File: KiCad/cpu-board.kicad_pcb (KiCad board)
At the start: 2 copper layers, 100 x 100 mm, 15 parts, among them SW1 SW_PUSH_SMALL, U1 29F040B, U10 74LS377, U11 GAL22V10, U2 68008D, U3 74LS00, U4 BS62LV4006, U5 74LS08, U6 74LS139, U7 74LS32, U8 74LS244, U9 LM555, X1 OSCILLATOR

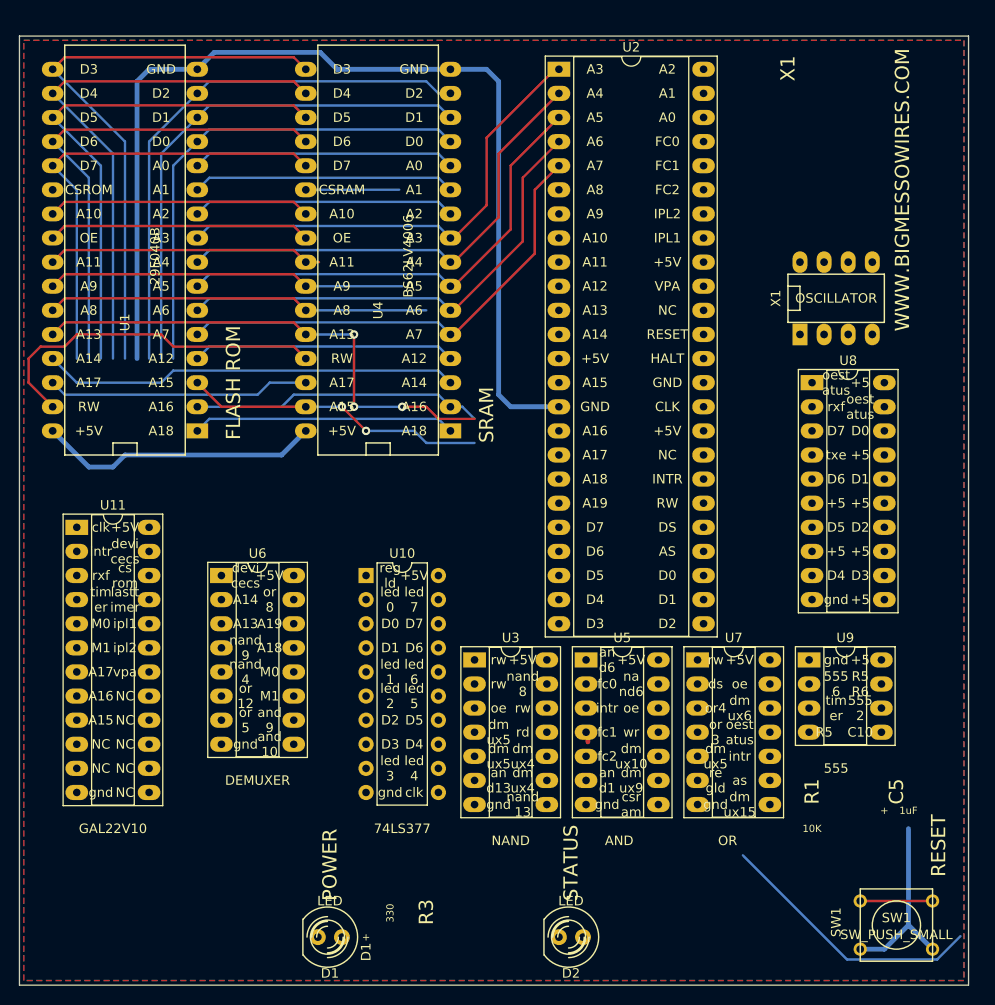
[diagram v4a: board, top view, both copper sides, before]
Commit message: add some address bus tracks
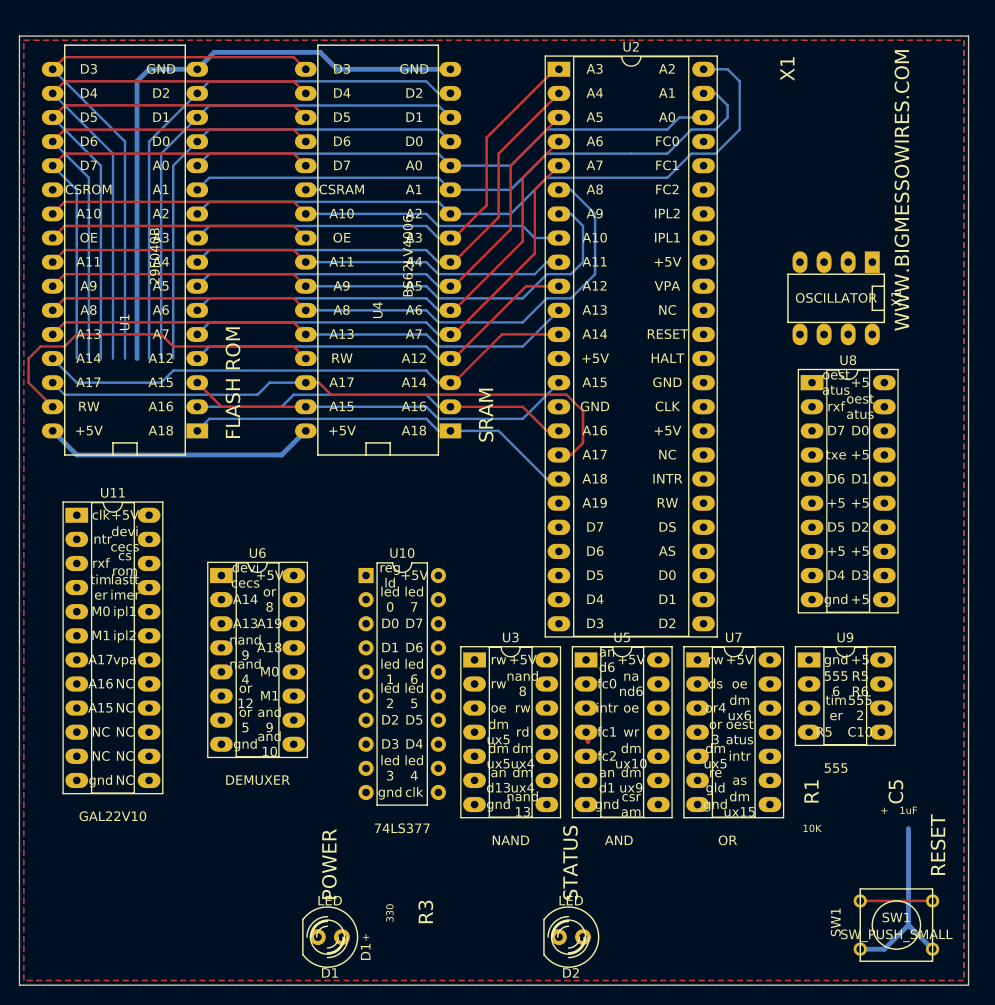
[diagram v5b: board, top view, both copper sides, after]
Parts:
- moved U11 1.27 mm to (66.0, 110.5)
- turned X1 to 180 degrees
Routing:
- net GND: track 129.6 -> 84.1 mm
- net /A2: track 27.7 -> 71.3 mm
- net /A17: track 27.7 -> 64.6 mm
- net /A1: track 27.7 -> 64.4 mm
- net /A8: track 40.4 -> 72.0 mm
- net /A0: track 27.7 -> 56.5 mm
- net Net-(U11-Pad13): track 28.5 -> 0.00 mm
- net /A9: track 37.9 -> 66.3 mm
- net /A10: track 27.7 -> 55.4 mm
- net /A11: track 29.1 -> 55.4 mm
- net /A12: track 27.7 -> 42.3 mm
- net /A18: track 27.7 -> 41.3 mm
- net /A14: track 44.0 -> 57.5 mm
- net /A15: track 31.8 -> 41.3 mm, vias 2 -> 0
- net /A16: track 30.8 -> 40.2 mm
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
